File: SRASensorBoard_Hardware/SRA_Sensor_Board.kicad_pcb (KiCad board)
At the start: 2 copper layers, 72 parts, among them J1 USB_A, Q1 BSS138, Q2 BSS138, Q3 BSS138, Q4 BSS138, U1 LT1910, U2 OKI, U3 OKI, U4 TM4C129E_Launchpad, U5 IRF7821PbF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

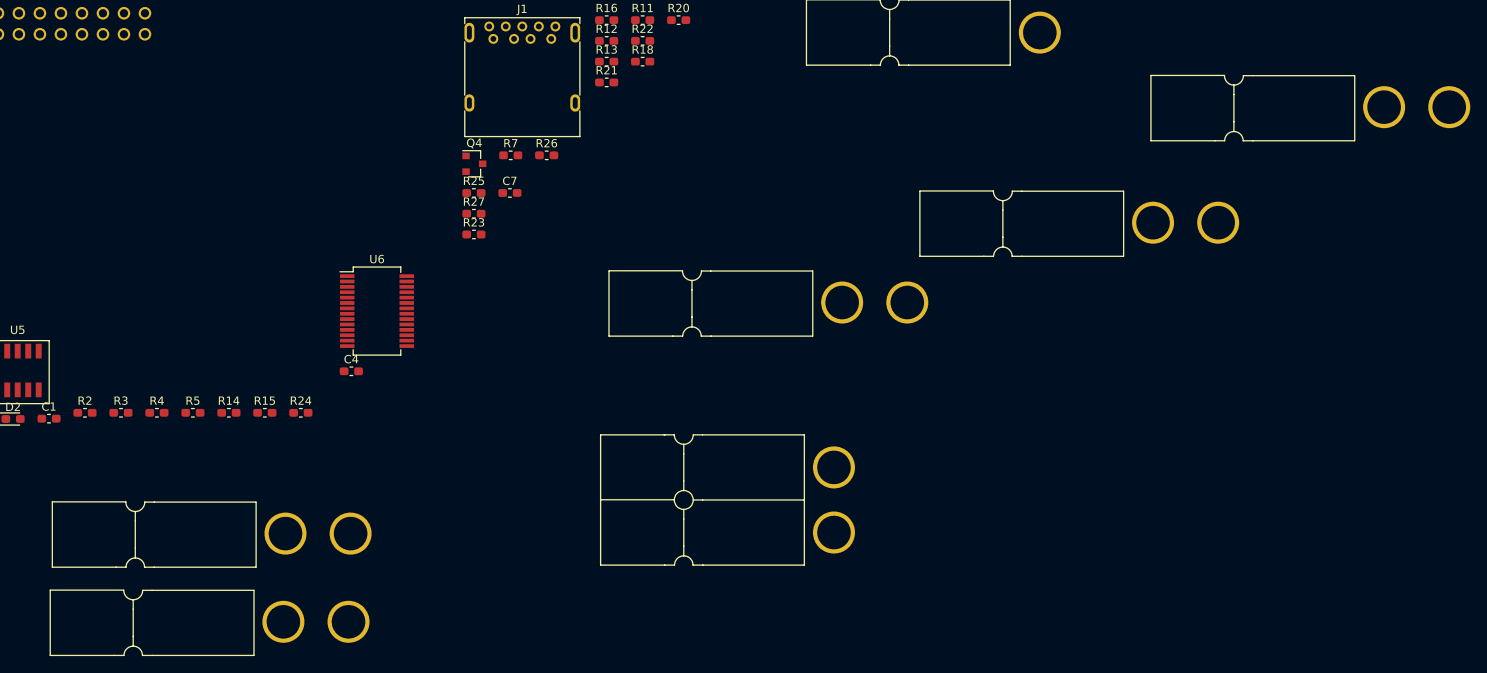
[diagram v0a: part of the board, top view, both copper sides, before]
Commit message: Board Genral Layout
General layout is done. Components are organized into groups for easier design.
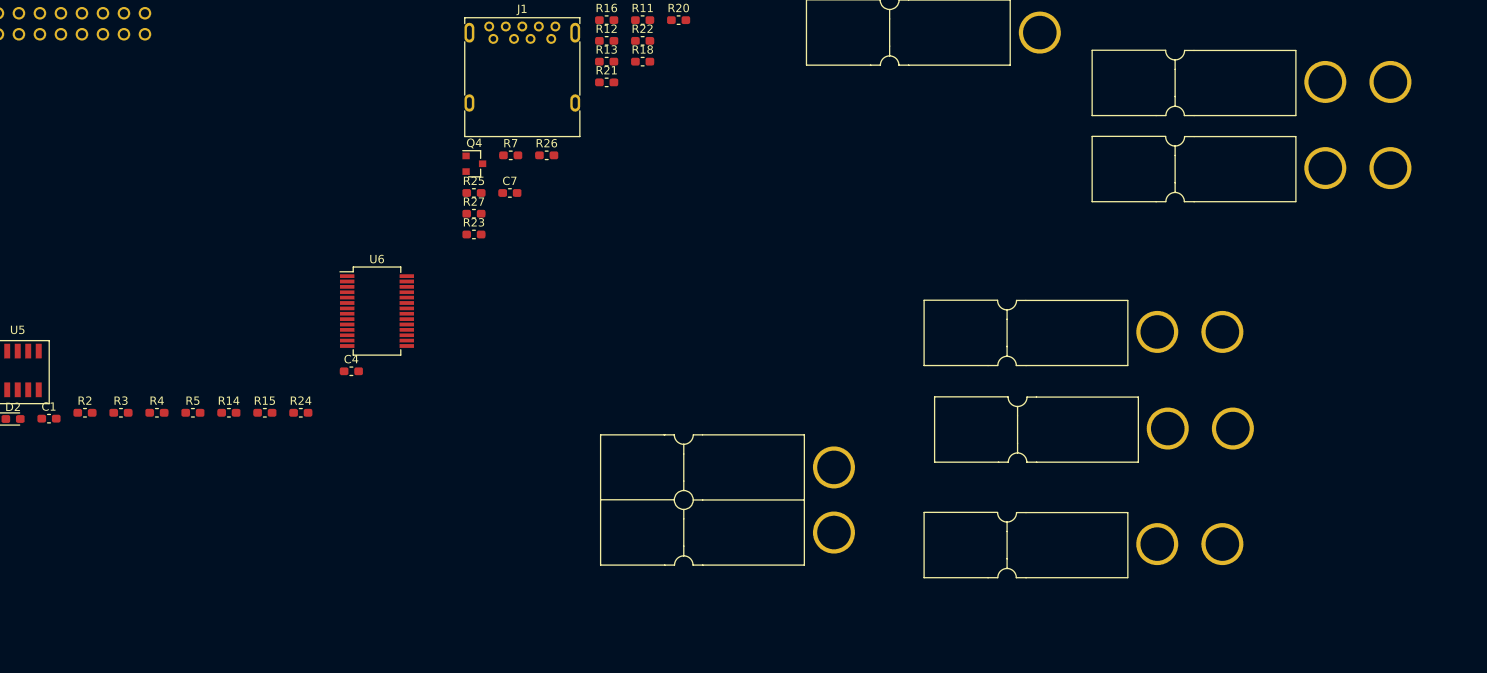
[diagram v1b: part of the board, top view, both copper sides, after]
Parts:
- Conn7: value Boost GND -> 12v Boost GND
- Conn8: value Boost GND -> 24v Boost GND
- moved Conn8 141.9 mm to (293.9, 101.9)
- moved Conn11 105.4 mm to (273.6, 157.7)
- moved Conn9 42.2 mm to (274.8, 143.8)
- moved Conn10 38.6 mm to (273.6, 132.1)
- moved Conn7 21.8 mm to (293.9, 112.3)
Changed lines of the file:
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@@
     (solder_mask_min_width 0.25)
     (aux_axis_origin 0 0)
-    (visible_elements FFFFF77F)
+    (visible_elements 7FFFF7FF)
     (pcbplotparams
       (layerselection 0x010fc_ffffffff)
@@
   )
   (module MRDT_Connectors:Anderson_2_Horizontal_Stacked (layer F.Cu)
-    (at 273.05 118.872)
+    (at 293.878 112.268)
     (fp_text reference Conn7 (at -5.461 4.826) (layer F.Fab) hide
       (effects (font (size 1 1) (thickness 0.15)))
     )
-    (fp_text value "Boost GND" (at -15.621 -4.699) (layer F.Fab)
+    (fp_text value "12v Boost GND" (at -15.621 -4.699) (layer F.Fab)
       (effects (font (size 1 1) (thickness 0.15)))
     )
@@
   )
   (module MRDT_Connectors:Anderson_2_Horizontal_Stacked (layer F.Cu)
-    (at 167.894 167.132)
+    (at 293.878 101.854)
     (fp_text reference Conn8 (at -5.461 4.826) (layer F.Fab) hide
       (effects (font (size 1 1) (thickness 0.15)))
     )
-    (fp_text value "Boost GND" (at -15.621 -4.699) (layer F.Fab)
+    (fp_text value "24v Boost GND" (at -15.621 -4.699) (layer F.Fab)
       (effects (font (size 1 1) (thickness 0.15)))
     )
@@
   )
   (module MRDT_Connectors:Anderson_2_Horizontal_Stacked (layer F.Cu)
-    (at 235.458 128.524)
+    (at 274.828 143.764)
     (fp_text reference Conn9 (at -5.461 4.826) (layer F.Fab) hide
       (effects (font (size 1 1) (thickness 0.15)))
@@
   )
   (module MRDT_Connectors:Anderson_2_Horizontal_Stacked (layer F.Cu)
-    (at 300.99 104.902)
+    (at 273.558 132.08)
     (fp_text reference Conn10 (at -5.461 4.826) (layer F.Fab) hide
       (effects (font (size 1 1) (thickness 0.15)))
@@
   )
   (module MRDT_Connectors:Anderson_2_Horizontal_Stacked (layer F.Cu)
-    (at 168.148 156.464)
+    (at 273.558 157.734)
     (fp_text reference Conn11 (at -5.461 4.826) (layer F.Fab) hide
       (effects (font (size 1 1) (thickness 0.15)))

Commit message: Tracing and whatnot
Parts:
- removed Conn10: UV_LED_V+_2, MRDT_Connectors:Anderson_2_Horizontal_Stacked
- removed Conn11: UV_LED_GND, MRDT_Connectors:Anderson_2_Horizontal_Stacked
- removed Conn8: 24v Boost GND, MRDT_Connectors:Anderson_2_Horizontal_Stacked
- removed Conn9: UV_LED_V+_1, MRDT_Connectors:Anderson_2_Horizontal_Stacked
- added G***: LOGO, MRDT_Silkscreens:0_MRDT_Logo_10mm, F.Cu at (186.7, 110.5)
- Conn5: value 12v Boost -> Boost 12V
- Conn6: value 24v Boost -> Boost 24V
- Conn7: value 12v Boost GND -> UV_led; footprint MRDT_Connectors:Anderson_2_Horizontal_Stacked -> MRDT_Connectors:Anderson_3_Horizontal_Side_by_Side
- R3, R4: footprint Resistor_SMD:R_0603_1608Metric_Pad1.05x0.95mm_HandSolder -> Resistor_THT:R_Axial_DIN0414_L11.9mm_D4.5mm_P15.24mm_Horizontal
- U1: footprint MRDT_ICs:SOIC127P599X175-8N -> custom:SOIC127P599X175-8N
- U5: footprint MRDT_ICs:IRF7821PBF -> custom:IRF7821PBF
- moved Conn7 176.7 mm to (124.5, 62.2), turned to 270 degrees
- moved R8 163.7 mm to (71.1, 80.9), turned to 270 degrees
- moved R10 155.7 mm to (78.7, 80.9), turned to 270 degrees
- moved R9 152.1 mm to (82.5, 80.9), turned to 270 degrees
- moved C2 140.1 mm to (83.8, 66.4), turned to 270 degrees
- moved R19 138.6 mm to (101.6, 91.0), turned to 270 degrees
- moved R22 137.3 mm to (74.9, 80.9), turned to 270 degrees
- moved R17 136.6 mm to (97.8, 80.9), turned to 270 degrees
- moved R13 136.1 mm to (71.1, 91.0), turned to 270 degrees
- moved R6 125.4 mm to (119.4, 81.7), turned to 270 degrees
- moved Q2 123.9 mm to (123.2, 82.5), turned to 180 degrees
- moved R7 122.0 mm to (74.9, 91.0), turned to 270 degrees
- moved R11 121.9 mm to (90.2, 80.9), turned to 270 degrees
- moved R12 121.7 mm to (86.4, 80.9), turned to 270 degrees
- moved J1 118.2 mm to (78.7, 67.3), turned to 270 degrees
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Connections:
- Conn5 pad 1: (no net) -> GND
- Conn6 pad 1: (no net) -> GND
- R3 pad 2: Net-(Conn9-Pad2) -> Net-(Conn7-Pad2)
- R4 pad 2: Net-(Conn10-Pad2) -> Net-(Conn7-Pad3)
- U1 pad 6: +12V -> +24V
- U1 pad 8: +12V -> +24V
- U4 pad PC4: C02_In -> TIVA_CO2_RX
- U4 pad PC5: C02_Out -> TIVA_CO2_TX
- U4 pad PK0: Flow_Receive -> TIVA_O2_RX
- U4 pad PK1: Flow_Output -> TIVA_O2_TX
- U4 pad PM3: Net-(U4-PadPM3) -> Reset
- U5 pad 5: +12V -> +24V
- U5 pad 6: +12V -> +24V
- U5 pad 7: +12V -> +24V
- U5 pad 8: +12V -> +24V
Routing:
- net +3V3: track 0.00 -> 254.5 mm, vias 0 -> 9
- net +5V: track 0.00 -> 243.9 mm, vias 0 -> 5
- net +12V: track 0.00 -> 192.8 mm, vias 0 -> 1
- net +24V: track 0.00 -> 155.7 mm
- net SW_ERROR: track 0.00 -> 102.9 mm, vias 0 -> 2
- net SW_Flag1: track 0.00 -> 94.0 mm, vias 0 -> 2
- net CCD_OS: track 0.00 -> 88.8 mm, vias 0 -> 4
- net SW_Flag2: track 0.00 -> 85.8 mm, vias 0 -> 3
- net O2_RX: track 0.00 -> 84.0 mm, vias 0 -> 2
- net TIVA_CO2_RX: track 0.00 -> 81.4 mm, vias 0 -> 2
- net LED_Enable: track 0.00 -> 78.6 mm, vias 0 -> 2
- net O2_TX: track 0.00 -> 77.8 mm, vias 0 -> 2
- net TIVA_CO2_TX: track 0.00 -> 72.3 mm, vias 0 -> 1
- net GND: track 0.00 -> 62.5 mm, vias 0 -> 7
- net CCD_INT1: track 0.00 -> 53.1 mm, vias 0 -> 3
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- added copper zone on B.Cu, net GND
- added copper zone on F.Cu, net GND
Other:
- board outline added: 124.5 x 81.3 mm
- board text added: "12V"
- board text added: "24V"
- board text added: "3V"
- board text added: "5V"
- board text added: "Buck Boost"
- board text added: "CCD I2"
- board text added: "GND"
- board text added: "I1"
- board text added: "I2"
- board text added: "Main PWR"
- board text added: "OS"
- board text added: "RX"
- board text added: "TX"
- board text added: "UV LED"
- board text added: "UV V+"

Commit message: Added Gerbs and whatnot
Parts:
- added G***: LOGO, custom:tetris_silkscreen, F.Cu at (71.8, 50.8)
- added G***: LOGO, footprints:Toni_Signature_Rev4, F.Cu at (175.3, 116.8)
- added G***: LOGO, custom:Don_Signature_Medium, F.Cu at (163.8, 116.8)
- Conn1: value Molex_SL_04 -> O2
- Conn3: value Molex_SL_04 -> CO2
- Conn4: value Molex_SL_05 -> CCD
- D10: value LED -> USB TX
- D11: value LED -> UV Enable
- D12: value LED -> CCD OS
- D13: value LED -> CCD 2
- D14: value LED -> CCD 1
- D15: value LED -> 12V
- D16: value LED -> O2 RX
- D17: value LED -> O2 TX
- D18: value LED -> CO2 TX
- D2: value LED -> 24V
- D3: value LED -> 3.3V
- D4: value LED -> 5V
- D5: value LED -> Flag 2
- D6: value LED -> Flag 1
- D7: value LED -> Error
- D8: value LED -> CO2 RX
- D9: value LED -> USB RX
- moved D10 25.0 mm to (71.1, 94.9)
- moved D7 25.0 mm to (94.0, 84.7)
- moved R13 25.0 mm to (94.0, 80.9)
- moved R16 25.0 mm to (71.1, 91.0)
- moved D9 15.2 mm to (74.9, 94.9)
- moved R15 15.2 mm to (74.9, 91.0)
- moved D16 7.62 mm to (82.5, 94.9)
- moved R7 7.62 mm to (82.5, 91.0)
- moved D18 3.81 mm to (86.4, 94.9)
- moved D8 3.81 mm to (90.2, 94.9)
- moved R14 3.81 mm to (90.2, 91.0)
- moved R24 3.81 mm to (86.4, 91.0)
- renumbered U3 to 3V, U2 to 5V
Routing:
- net +3V3: track 254.5 -> 298.3 mm, vias 9 -> 11
- net SW_ERROR: track 102.9 -> 84.6 mm
- net TIVA_USB_TX: track 42.9 -> 57.7 mm
- net TIVA_USB_RX: track 45.7 -> 60.4 mm
- net +5V: track 243.9 -> 258.4 mm, vias 5 -> 6
- net O2_RX: track 84.0 -> 76.8 mm
- net C02_TX: track 53.1 -> 48.8 mm
- net C02_RX: track 42.1 -> 38.4 mm
- net +12V: track 192.8 -> 195.4 mm
- net GND: track 62.5 -> 65.0 mm
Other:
- board text added: "CCD"
- board text added: "CO2"
- board text added: "Methane"
- board text added: "O2"
- board text added: "Power"
- board text added: "Sensor Board, Rev 2 Mars Rover, 2020 Missouri S&T Don Shaw, Toni Ramljak"
- board text added: "Software"
- board text added: "UV"

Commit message: PRR Changes
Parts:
- removed U1: LT1910, custom:SOIC127P599X175-8N
- removed U5: IRF7821PbF, custom:IRF7821PBF
- added Q5: Q_PMOS_GDS, Package_TO_SOT_SMD:TO-252-2, F.Cu at (155.2, 65.5)
- added Q6: Q_NMOS_GSD, Package_TO_SOT_SMD:SOT-23, F.Cu at (144.5, 63.2)
- added R28: 22k, Resistor_SMD:R_0603_1608Metric_Pad1.05x0.95mm_HandSolder, F.Cu at (162.8, 68.0)
- added R29: 22k, Resistor_SMD:R_0603_1608Metric_Pad1.05x0.95mm_HandSolder, F.Cu at (147.7, 63.3)
- added R30: 10k, Resistor_SMD:R_0603_1608Metric_Pad1.05x0.95mm_HandSolder, F.Cu at (141.0, 63.3)
- D11: value UV Enable -> Enable
- D3: value 3.3V -> 3v3
- R11, R12, R13, R14, R15, R16, R17, R18, R19, R20, R23, R24, R7: value 510 -> 330
- moved Conn7 20.0 mm to (104.8, 58.7)
- renumbered 5V to U2, 3V to U3
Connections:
- net USB_RX renamed Net-(U6-Pad23)
- net USB_TX renamed Net-(U6-Pad22)
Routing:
- net +24V: track 155.7 -> 130.8 mm
- net Net-(Q5-Pad1): track 0.00 -> 20.7 mm
- net Net-(U1-Pad5): track 10.1 -> 0.00 mm
- net Net-(Q5-Pad2): track 30.5 -> 35.9 mm
- net +12V: track 195.4 -> 199.6 mm
- net Net-(Q6-Pad3): track 0.00 -> 2.60 mm
- net LED_Enable: track 78.6 -> 76.9 mm
- added copper zone on F.Cu, net +24V
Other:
- outline, holes or cut-outs redrawn
- board text added: "3v3"
- board text removed: "CCD I2"

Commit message: PRR Changes prt 2
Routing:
- net GND: track 65.0 -> 69.8 mm, vias 7 -> 30
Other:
- board text added: "Sensor Board, Rev 1 Mars Rover, 2020 Missouri S&T Don Shaw, Toni Ramljak"
- board text removed: "Sensor Board, Rev 2 Mars Rover, 2020 Missouri S&T Don Shaw, Toni Ramljak"

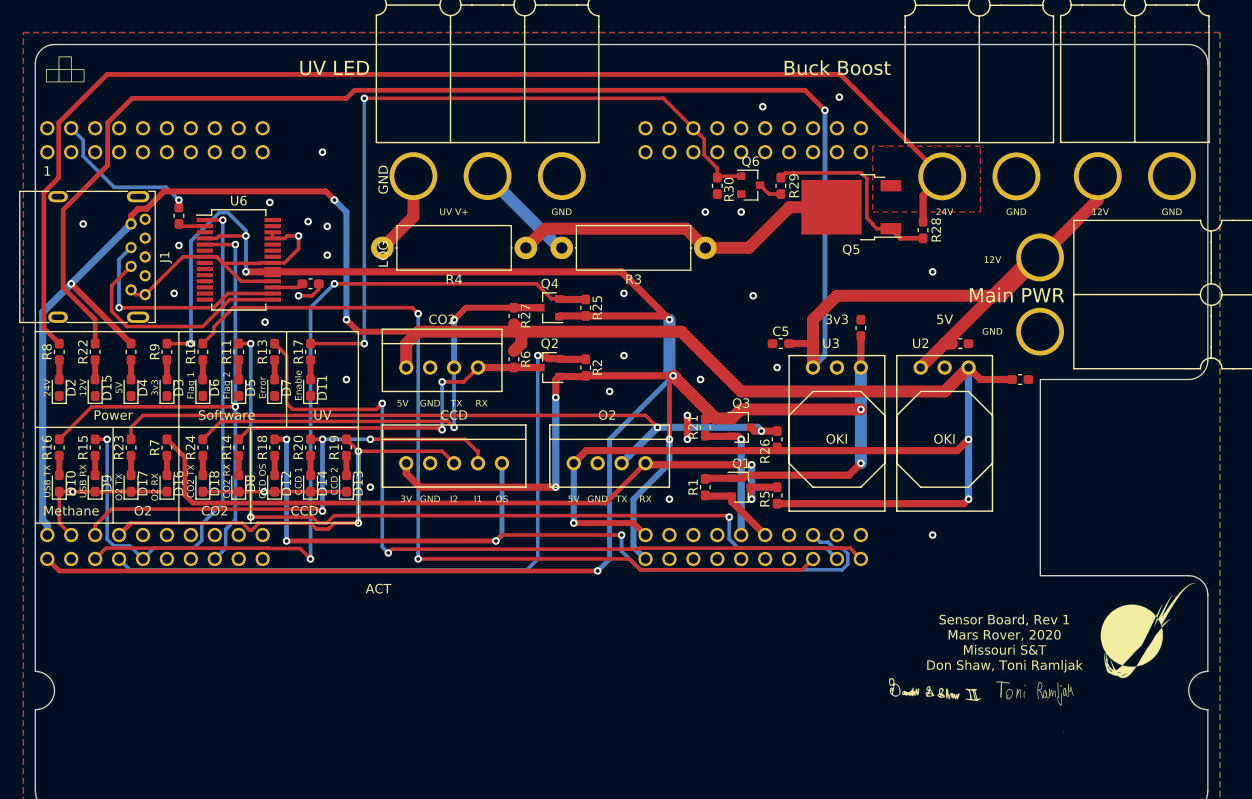
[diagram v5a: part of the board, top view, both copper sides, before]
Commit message: Rev 2
Changed to a FT230XS due to communication problems.
Moved the power resistors because they looked a little to close to
microcontroller components.
Made some labels more visible.
Changed the footprint for the usb to be correct with the component.
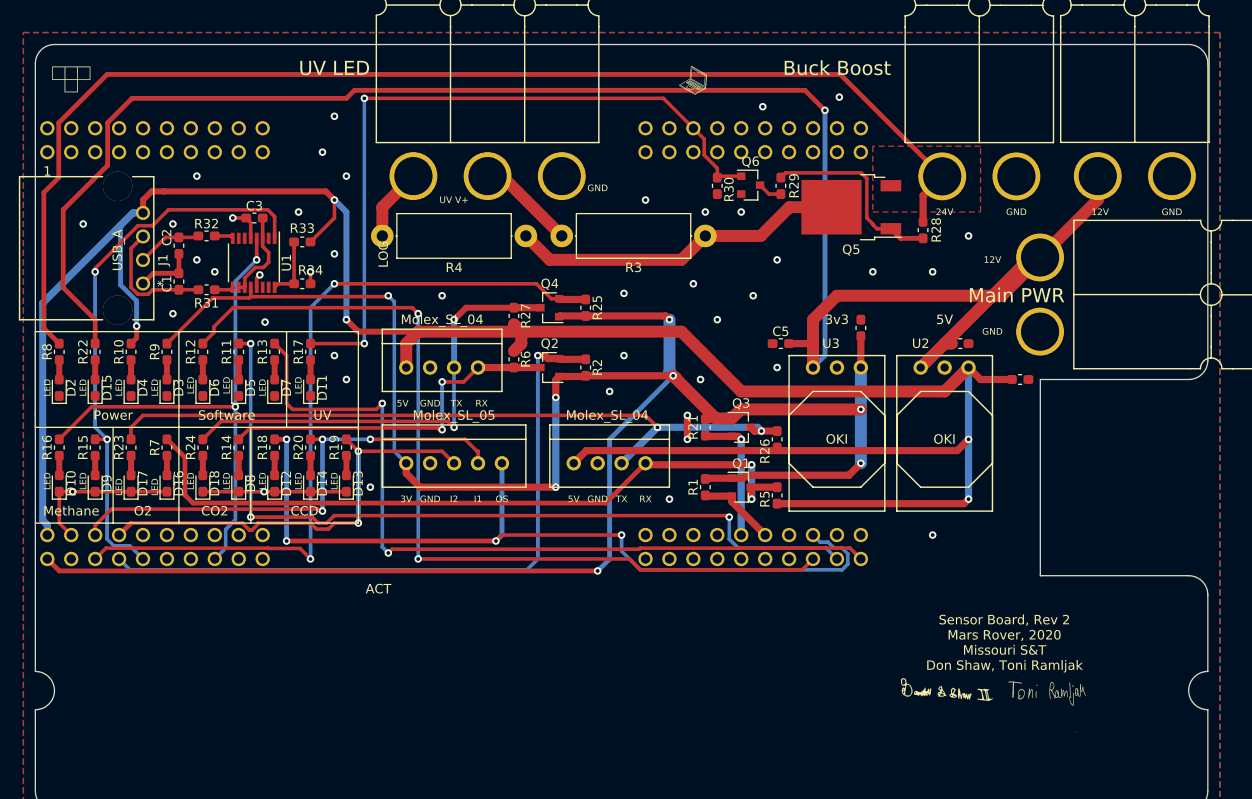
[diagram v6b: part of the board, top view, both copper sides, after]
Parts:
- removed the G*** at (186.7, 110.5)
- removed U6: FT232RL, Package_SO:SSOP-28_5.3x10.2mm_P0.65mm
- added C3: 100nf, Capacitor_SMD:C_0603_1608Metric_Pad1.05x0.95mm_HandSolder, F.Cu at (91.8, 66.7)
- added G***: LOGO, custom:laptop_medium, F.Cu at (138.4, 52.1)
- added R31: 27, Resistor_SMD:R_0603_1608Metric_Pad1.05x0.95mm_HandSolder, F.Cu at (86.8, 74.3)
- added R32: 27, Resistor_SMD:R_0603_1608Metric_Pad1.05x0.95mm_HandSolder, F.Cu at (86.8, 68.6)
- added R33: 4.7k, Resistor_SMD:R_0603_1608Metric_Pad1.05x0.95mm_HandSolder, F.Cu at (96.9, 69.2)
- added R34: 10k, Resistor_SMD:R_0603_1608Metric_Pad1.05x0.95mm_HandSolder, F.Cu at (96.9, 73.7)
- added U1: FT230XS, Package_SO:SSOP-16_3.9x4.9mm_P0.635mm, F.Cu at (91.8, 71.4)
- C1: value 0.1 uF -> 47pF
- C2: value .1 uF -> 47pF
- Conn1: value O2 -> Molex_SL_04
- Conn3: value CO2 -> Molex_SL_04
- Conn4: value CCD -> Molex_SL_05
- D10: value USB TX -> LED
- D11: value Enable -> LED
- D12: value CCD OS -> LED
- D13: value CCD 2 -> LED
- D14: value CCD 1 -> LED
- D15: value 12V -> LED
- D16: value O2 RX -> LED
- D17: value O2 TX -> LED
- D18: value CO2 TX -> LED
- D2: value 24V -> LED
- D3: value 3v3 -> LED
- D4: value 5V -> LED
- D5: value Flag 2 -> LED
- D6: value Flag 1 -> LED
- D7: value Error -> LED
- D8: value CO2 RX -> LED
- D9: value USB RX -> LED
- J1: footprint Connector_USB:USB3_A_Molex_48393-001 -> custom:292303-1
- moved C1 14.0 mm to (83.8, 73.4), turned to 90 degrees
- moved J1 7.13 mm to (82.0, 73.6)
- moved C2 3.17 mm to (83.8, 69.6)
- moved G*** 1.42 mm to (72.4, 52.1), turned to 0 degrees
- moved G*** 1.27 mm to (176.5, 116.8)
- moved R3 1.27 mm to (139.7, 68.6)
- moved R4 1.27 mm to (120.7, 68.6)
- moved G*** 1.27 mm to (165.1, 116.8)
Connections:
- C1 pad 1: Net-(C1-Pad1) -> USB_Data-
- C2 pad 1: Reset -> USB_Data+
- C2 pad 2: Net-(C2-Pad2) -> GND
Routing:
- net +3V3: track 298.1 -> 244.9 mm, vias 11 -> 8
- net GND: track 69.8 -> 47.2 mm, vias 30 -> 42
- net USB_Data+: track 24.6 -> 6.93 mm
- net Reset: track 16.4 -> 0.00 mm, vias 1 -> 0
- net USB_Data-: track 23.8 -> 13.6 mm, vias 1 -> 0
- net Net-(C3-Pad1): track 0.00 -> 9.81 mm
- net Net-(R33-Pad1): track 0.00 -> 6.66 mm
- net +5V: track 258.4 -> 254.8 mm, vias 6 -> 5
- net Net-(C1-Pad1): track 3.30 -> 0.00 mm
- net Net-(C2-Pad2): track 2.85 -> 0.00 mm
- net Net-(R31-Pad1): track 0.00 -> 2.01 mm
- net Net-(R32-Pad1): track 0.00 -> 2.01 mm
- net TIVA_USB_TX: track 57.7 -> 56.0 mm
- net Net-(Conn7-Pad3): track 8.99 -> 7.72 mm
- net TIVA_USB_RX: track 60.4 -> 59.4 mm
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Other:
- board text added: "Sensor Board, Rev 2 Mars Rover, 2020 Missouri S&T Don Shaw, Toni Ramljak"
- board text removed: "Sensor Board, Rev 1 Mars Rover, 2020 Missouri S&T Don Shaw, Toni Ramljak"
